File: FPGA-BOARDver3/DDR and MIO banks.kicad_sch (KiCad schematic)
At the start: 1 part, among them U1 XC7Z020-1CLG400I__

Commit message: spdif fpga bansks
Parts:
- added C4: 100nF, footprints:C_0402, symbol Device:C
- added C5, C8, C9: 10nF, footprints:C_0402, symbol Device:C
- added J4: Conn_01x04_Pin, footprints:CONN_PZ254V-11-04P_XFC, symbol Connector:Conn_01x04_Pin
- added J5, J8: Conn_01x02_Pin, footprints:CONN_PZ254V-11-02P_02P_XFC, symbol Connector:Conn_01x02_Pin
- added R17, R18, R19, R20: 10K 1%, footprints:R_0402, symbol Device:R_US
- added R36, R37, R38, R40, R42, R48, R49: 20K, footprints:R_0402, symbol Device:R_US
- added R39, R41, R43, R44, R45, R46, R47: 1K, footprints:R_0402, symbol Device:R_US
- added R4: 40.2, footprints:R_0402, symbol Device:R_US
- added R5, R6, R7: 80.6 1%, footprints:R_0402, symbol Device:R_US
- added R50, R51: 49.9, footprints:R_0402, symbol Device:R_US
- added R8: 40.2 1%, footprints:R_0402, symbol Device:R_US
- added S2: PTS645SK50SMTR92LFS, footprints:SW_PTS645SK50SMTR92LFS, symbol PTS645SK50SMTR92LFS:PTS645SK50SMTR92LFS
- added U2: DSC1122CI5-050.0000T, footprints:VDFN6_3P2X2P5_MCH, symbol 2025-04-06_19-32-54:DSC1122CI5-050.0000T
- added U3: NC7WZ07P6X, footprints:NC7WZ07P6X, symbol NC7WZ07P6X:NC7WZ07P6X
- U1: footprint footprints:CLG400_ZYNQ-7000_AMD -> XC7Z020-1CLG400I:CLG400_ZYNQ-7000_AMD
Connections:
- net DDR3_DM1: now reaches U1.A1 (PS_DDR_DM0_502)
- net DDR3_D15: now reaches U1.A2 (PS_DDR_DQ2_502)
- net DDR3_D13: now reaches U1.A4 (PS_DDR_DQ3_502)
- net DDR3_DQS1_N: now reaches U1.B2 (PS_DDR_DQS_N0_502)
- net DDR3_D12: now reaches U1.B3 (PS_DDR_DQ1_502)
- net DDR3_RESET: now reaches U1.B4 (PS_DDR_DRST_B_502)
- net DDR3_D14: now reaches U1.C1 (PS_DDR_DQ6_502)
- net DDR3_DQS1_P: now reaches U1.C2 (PS_DDR_DQS_P0_502)
- net DDR3_D11: now reaches U1.C3 (PS_DDR_DQ0_502)
- net DDR3_D10: now reaches U1.D1 (PS_DDR_DQ5_502)
- net DDR3_D9: now reaches U1.D3 (PS_DDR_DQ4_502)
- net DDR3_A13: now reaches U1.D4 (PS_DDR_A13_502)
- net DDR3_D8: now reaches U1.E1 (PS_DDR_DQ7_502)
- net DDR3_D2: now reaches U1.E2 (PS_DDR_DQ8_502)
- net DDR3_D0: now reaches U1.E3 (PS_DDR_DQ9_502)
- net DDR3_A12: now reaches U1.E4 (PS_DDR_A12_502)
- net DDR3_DM0: now reaches U1.F1 (PS_DDR_DM1_502)
- net DDR3_DQS0_N: now reaches U1.F2 (PS_DDR_DQS_N1_502)
- net DDR3_A14: now reaches U1.F4 (PS_DDR_A14_502)
- net DDR3_A10: now reaches U1.F5 (PS_DDR_A10_502)
- net DDR3_DQS0_P: now reaches U1.G2 (PS_DDR_DQS_P1_502)
- net DDR3_D6: now reaches U1.G3 (PS_DDR_DQ10_502)
- net DDR3_A11: now reaches U1.G4 (PS_DDR_A11_502)
- net at U1.G5 (PS_DDR_VRN_502): now also R6.2
- net DDR3_D3: now reaches U1.H1 (PS_DDR_DQ14_502)
- net DDR3_D7: now reaches U1.H2 (PS_DDR_DQ13_502)
- net DDR3_D1: now reaches U1.H3 (PS_DDR_DQ11_502)
- net at U1.H5 (PS_DDR_VRP_502): now also R7.2
- net DDR3_VREF: now reaches U1.H6 (PS_DDR_VREF0_502)
- net DDR3_VREF: now also U1.P6 (PS_DDR_VREF1_502), C4.1, C5.1, R17.2, R20.1
- net DDR3_D5: now reaches U1.J1 (PS_DDR_DQ15_502)
- net DDR3_D4: now reaches U1.J3 (PS_DDR_DQ12_502)
- net DDR3_A9: now reaches U1.J4 (PS_DDR_A9_502)
- net DDR3_BA2: now reaches U1.J5 (PS_DDR_BA2_502)
- net DDR3_A8: now reaches U1.K1 (PS_DDR_A8_502)
- net DDR3_A1: now reaches U1.K2 (PS_DDR_A1_502)
- net DDR3_A3: now reaches U1.K3 (PS_DDR_A3_502)
- net DDR3_A7: now reaches U1.K4 (PS_DDR_A7_502)
- net DDR3_A5: now reaches U1.L1 (PS_DDR_A5_502)
- net DDR3_CK_P: now reaches U1.L2 (PS_DDR_CKP_502)
- net DDR3_CK_P: now also R5.1
- net DDR3_A6: now reaches U1.L4 (PS_DDR_A6_502)
- net DDR3_BA0: now reaches U1.L5 (PS_DDR_BA0_502)
- net DDR3_CK_N: now reaches U1.M2 (PS_DDR_CKN_502)
- net DDR3_CK_N: now also R5.2
- net DDR3_A2: now reaches U1.M3 (PS_DDR_A2_502)
- net DDR3_A4: now reaches U1.M4 (PS_DDR_A4_502)
- net DDR3_WE: now reaches U1.M5 (PS_DDR_WE_B_502)
- net DDR3_CS: now reaches U1.N1 (PS_DDR_CS_B_502)
- net DDR3_A0: now reaches U1.N2 (PS_DDR_A0_502)
- net DDR3_CK0: now reaches U1.N3 (PS_DDR_CKE_502)
- net DDR3_ODT0: now reaches U1.N5 (PS_DDR_ODT_502)
- net DDR3_RAS: now reaches U1.P4 (PS_DDR_RAS_B_502)
- net DDR3_CAS: now reaches U1.P5 (PS_DDR_CAS_B_502)
- net DDR3_BA1: now reaches U1.R4 (PS_DDR_BA1_502)
- net USBHOST_DATA5: now reaches U1.A10 (PS_MIO37_501)
- net USBHOST_CLK: now reaches U1.A11 (PS_MIO36_501)
- net USBHOST_DATA2: now reaches U1.A12 (PS_MIO34_501)
- net USBHOST_DATA0: now reaches U1.A14 (PS_MIO32_501)
- net ETH_RXD3: now reaches U1.A15 (PS_MIO26_501)
- net ETH_RXD1: now reaches U1.A16 (PS_MIO24_501)
- net ETH_TXD3: now reaches U1.A17 (PS_MIO20_501)
- net ETH_TXCLK: now reaches U1.A19 (PS_MIO16_501)
- net SD_D1: now reaches U1.A9 (PS_MIO43_501)
- net PS_RST: now reaches U1.B10 (PS_SRST_B_501)
- net PS_RST: now also R43.2, R44.2, U3.3 (A2)
- net SD_CD: now reaches U1.B14 (PS_MIO47_501)
- net SD_D3: now reaches U1.B15 (PS_MIO45_501)
- net ETH_RXCK: now reaches U1.B17 (PS_MIO22_501)
- net ETH_TXD1: now reaches U1.B18 (PS_MIO18_501)
- net ETH_MDC: now reaches U1.C10 (PS_MIO52_501)
- net ETH_MDIO: now reaches U1.C11 (PS_MIO53_501)
- net USBHOST_DIR: now reaches U1.C13 (PS_MIO29_501)
- net USBHOST_STP: now reaches U1.C15 (PS_MIO30_501)
- net USBHOST_DATA4: now reaches U1.C16 (PS_MIO28_501)
- net SD_CMD: now reaches U1.C17 (PS_MIO41_501)
- net USBHOST_DATA7: now reaches U1.C18 (PS_MIO39_501)
- net ETH_TXD2: now reaches U1.D10 (PS_MIO19_501)
- net ETH_RXD0: now reaches U1.D11 (PS_MIO23_501)
- net ETH_RXCTL: now reaches U1.D13 (PS_MIO27_501)
- net at U1.D14 (PS_MIO40_501): now also R8.1
- net USBHOST_DATA1: now reaches U1.D15 (PS_MIO33_501)
- net USBHOST_RESETN: now reaches U1.D16 (PS_MIO46_501)
- net VREF0V9: now reaches U1.E11 (PS_MIO_VREF_501)
- net VREF0V9: now also C8.1, R18.2, R19.1
- net SD_D0: now reaches U1.E12 (PS_MIO42_501)
- net USBHOST_DATA6: now reaches U1.E13 (PS_MIO38_501)
- net ETH_TXD0: now reaches U1.E14 (PS_MIO17_501)
- net USBHOST_NXT: now reaches U1.E16 (PS_MIO31_501)
- net USBHOST_DATA3: now reaches U1.F12 (PS_MIO35_501)
- net SD_D2: now reaches U1.F13 (PS_MIO44_501)
- net ETH_TXCTL: now reaches U1.F14 (PS_MIO21_501)
- net ETH_RXD2: now reaches U1.F15 (PS_MIO25_501)
- net at U1.A5 (PS_MIO6_500): now also R4.1
- net SPI_DQ3/MODE0: now reaches U1.A6 (PS_MIO5_500)
- net SPI_DQ3/MODE0: now also R48.1
- net SPI_CS: now reaches U1.A7 (PS_MIO1_500)
- net ETH_RST_B: now reaches U1.B5 (PS_MIO9_500)
- net SPI_DQ2/MODE2: now reaches U1.B7 (PS_MIO4_500)
- net SPI_DQ2/MODE2: now also R49.1
- net SPI_DQ0/MODE3: now reaches U1.B8 (PS_MIO2_500)
- net SPI_DQ0/MODE3: now also R40.2
- net UART_TXD_IN: now reaches U1.C5 (PS_MIO14_500)
- net USBHOST_OC: now reaches U1.C6 (PS_MIO11_500)
- net PS_POR_B: now reaches U1.C7 (PS_POR_B_500)
- net UART_RXD_OUT: now reaches U1.C8 (PS_MIO15_500)
- net SPI_SCLK_FB/VCFG1: now reaches U1.D5 (PS_MIO8_500)
- net SPI_SCLK_FB/VCFG1: now also R36.2
- net SPIDQ1/MODE1: now reaches U1.D6 (PS_MIO3_500)
- net VCFG0: now reaches U1.D8 (PS_MIO7_500)
- net VCFG0: now also R37.2
- net CK_RST: now reaches U1.D9 (PS_MIO12_500)
- net CK_RST: now also R45.1, U3.4 (Y2)
- net PS_CLK: now reaches U1.E7 (PS_CLK_500)
- net PS_CLK: now also R50.1
- net ETH_INT_B: now reaches U1.E9 (PS_MIO10_500)
- new net: J4.3 (Pin_3), R47.2, R49.2
- new net: J8.1 (Pin_1), R41.2, R42.1
- new net: R50.2, R51.2, U2.4 (OUT)
- new net: J4.1 (Pin_1), R46.1, R48.2
- new net: R44.1, S2.1
- new net: J5.1 (Pin_1), R39.2, R40.1
- new net +1V5: R17.1, R7.1
- new net +1V8: R18.1, R43.1
- new net +3V3: C9.1, J4.4 (Pin_4), J5.2 (Pin_2), R36.1, R45.2, R46.2, U2.1 (EN), U2.6 (VDD)
- new net ETH_CLK: R51.1
- new net GNDREF: C4.2, C5.2, C8.2, C9.2, J4.2 (Pin_2), R19.2, R20.2, R37.1, R38.1, R39.1, R41.1, R47.1, R6.1, S2.3, U2.3 (GND)
- new net SD_CCLK: R8.2
- new net SPI_DQ1/MODE1: R38.2
- new net SPI_SCK_MODE4: R4.2
- new net SPI_SCK/MODE4: R42.2

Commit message: All pages complete , pi header left
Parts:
- removed S2: PTS645SK50SMTR92LFS, footprints:SW_PTS645SK50SMTR92LFS, symbol PTS645SK50SMTR92LFS:PTS645SK50SMTR92LFS
- added S2: PTS645SK50SMTR92LFS, footprints:SW_PTS645SK50SMTR92LFS, symbol PTS645SK50SMTR92LFS_:PTS645SK50SMTR92LFS
- U1: footprint XC7Z020-1CLG400I:CLG400_ZYNQ-7000_AMD -> footprints:CLG400_ZYNQ-7000_AMD
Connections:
- net GNDREF: now also S2.3
- net at R44.1: now also S2.1
- new net VCC: U3.5 (VCC)

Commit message: update
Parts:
- removed U3: NC7WZ07P6X, footprints:NC7WZ07P6X, symbol NC7WZ07P6X:NC7WZ07P6X
- added C176: 100nF, footprints:C_0402, symbol Device:C
- added U23: NC7WZ07P6X, footprints:NC7WZ07P6X, symbol NC7WZ07P6X:NC7WZ07P6X_modified
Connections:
- net +3V3: now also C176.1, U23.5 (VCC)
- net CK_RST: now also U23.4 (Y2)
- net GNDREF: now also C176.2, U23.2 (GND)
- net PS_RST: now also U23.3 (A2)
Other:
- note added: "VCC1V5"
- note added: "VCC1V8_IO"
- note added: "VCC3V3"

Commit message: schematic pages for review
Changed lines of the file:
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@@
 		(fields_autoplaced yes)
 		(property "Reference" "U23"
-			(at 267.97 155.5749 0)
-			(effects
-				(font
-					(size 1.27 1.27)
-				)
-				(justify left)
+			(at 269.24 140.97 0)
+			(effects
+				(font
+					(size 1.27 1.27)
+				)
 			)
 		)
 		(property "Value" "NC7WZ07P6X"
-			(at 267.97 158.1149 0)
-			(effects
-				(font
-					(size 1.27 1.27)
-				)
-				(justify left)
+			(at 269.24 143.51 0)
+			(effects
+				(font
+					(size 1.27 1.27)
+				)
 			)
 		)
@@
 	)
 	(symbol
+		(lib_name "NC7WZ07P6X_modified_1")
 		(lib_id "NC7WZ07P6X:NC7WZ07P6X_modified")
 		(at 246.38 146.05 0)

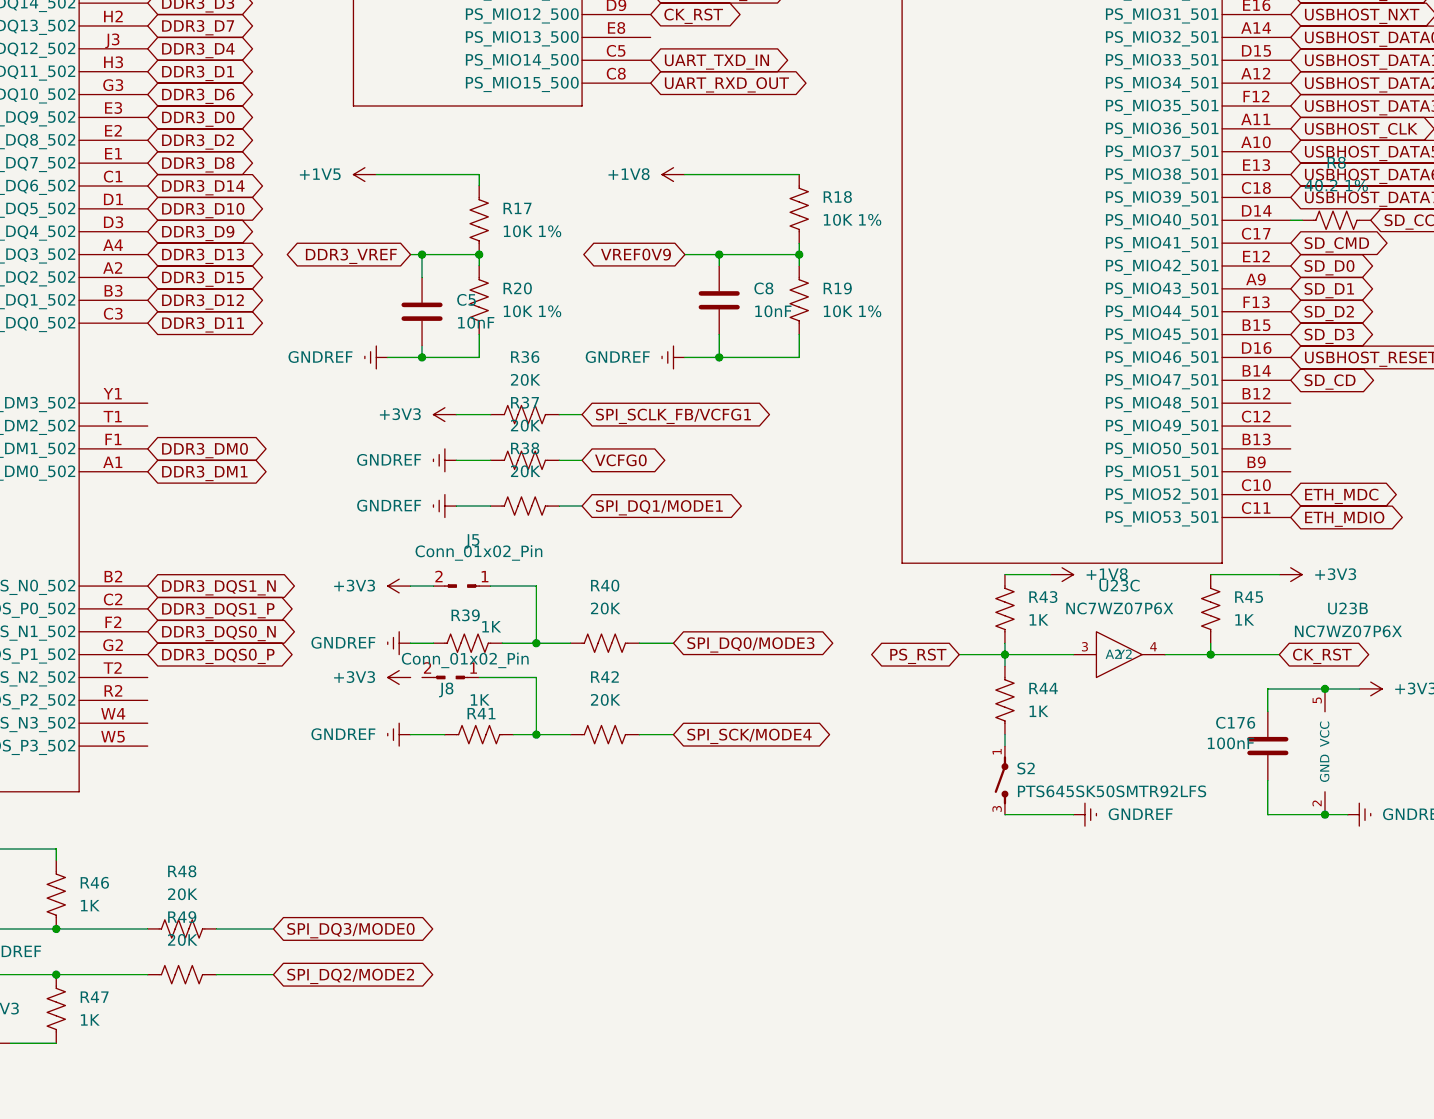
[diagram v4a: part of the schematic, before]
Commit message: added audio out and usb
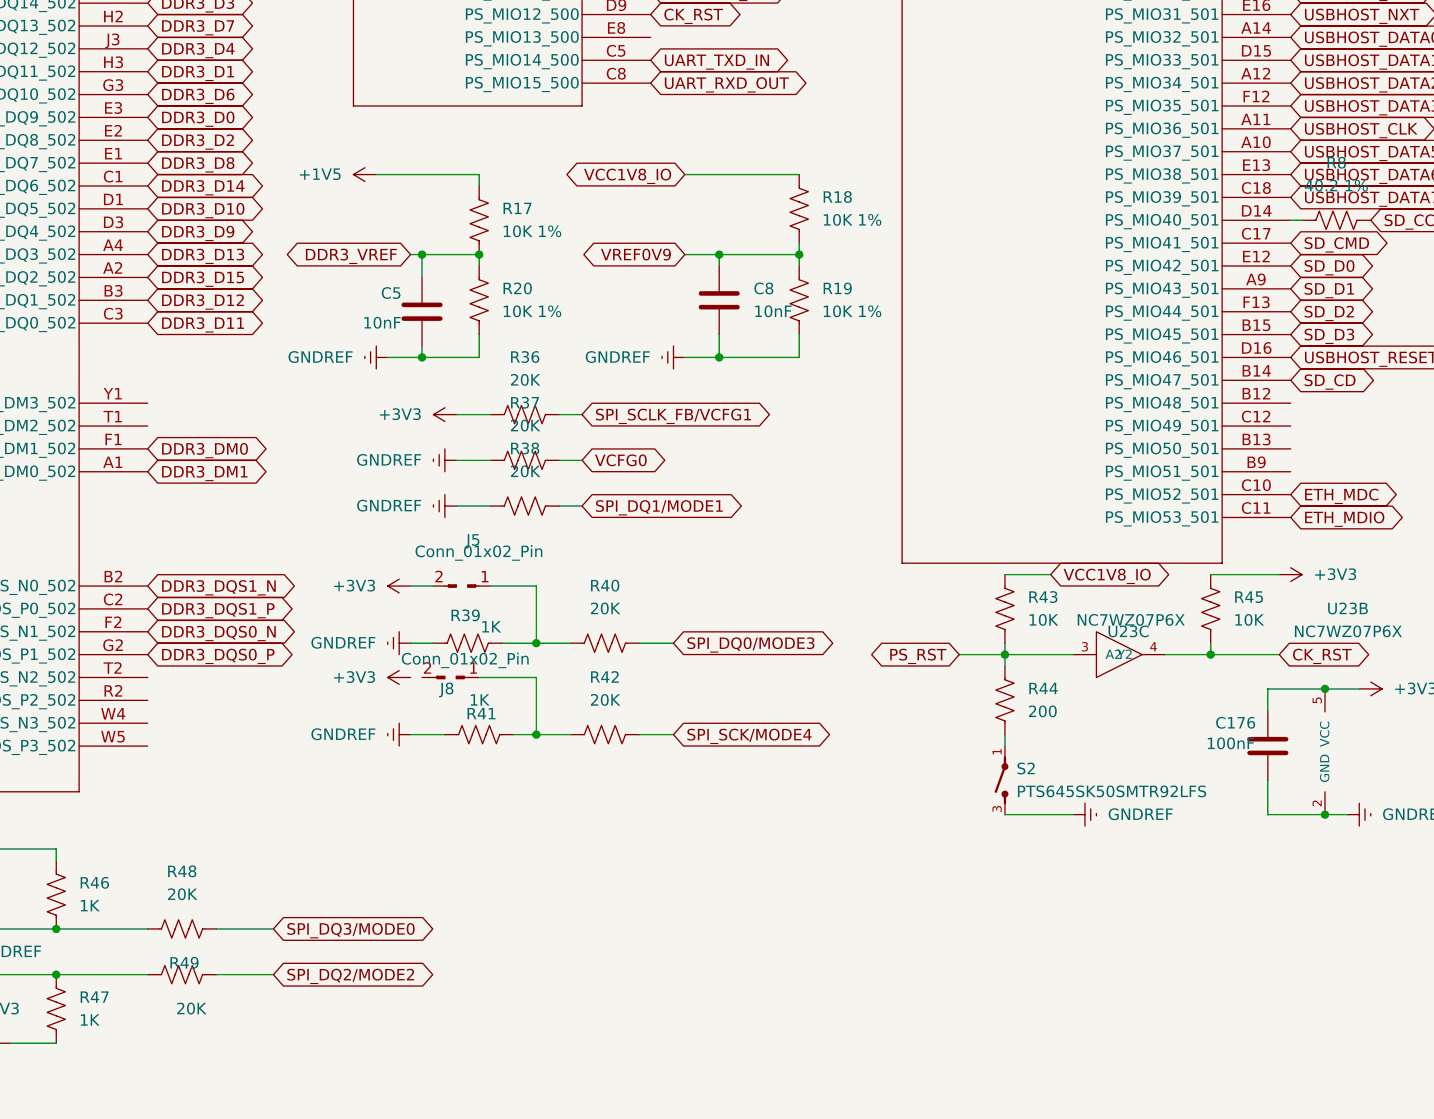
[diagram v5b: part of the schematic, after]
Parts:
- R43, R45: value 1K -> 10K
- R44: value 1K -> 200
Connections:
- net +1V8 renamed VCC1V8_IO

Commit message: updated schematic and layout
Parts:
- removed R51: 49.9, footprints:R_0402, symbol Device:R_US
- removed U2: DSC1122CI5-050.0000T, footprints:VDFN6_3P2X2P5_MCH, symbol 2025-04-06_19-32-54:DSC1122CI5-050.0000T
- added R234, R235, R236, R237, R238, R239: 40.2, footprints:R_0402, symbol Device:R_US
- added Y2: SG-8018CE_50.0000M-TJHPA, footprints:OSC_SG-8018CE_50.0000M-TJHPA, symbol SG-8018CE_50.0000M-TJHPA:SG-8018CE_50.0000M-TJHPA
- C176, C4: LCSC PN (none) -> c1525
- C5, C8, C9: LCSC PN (none) -> c15195
- J4: footprint footprints:CONN_PZ254V-11-04P_XFC -> footprints:PinHeader_1x04_P2.54mm_Vertical; LCSC PN (none) -> digi/mouser
- J5, J8: footprint footprints:CONN_PZ254V-11-02P_02P_XFC -> footprints:PinHeader_1x02_P2.54mm_Vertical; LCSC PN (none) -> digi/mouser
- R17, R18, R19, R20, R43, R45: LCSC PN (none) -> C60490
- R36, R37, R38, R40, R42, R48, R49: LCSC PN (none) -> C93942
- R39, R41, R46, R47: LCSC PN (none) -> C106235
- R4, R8: LCSC PN (none) -> C274892
- R44: LCSC PN (none) -> C114764
- R5, R6, R7: LCSC PN (none) -> C843839
- R50: LCSC PN (none) -> C87044
- S2: LCSC PN (none) -> mouser
- U1: LCSC PN (none) -> C1519081
- U23: LCSC PN (none) -> C95342
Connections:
- net SPIDQ1/MODE1 is gone; now on net SPI_DQ1/MODE1: U1.D6 (PS_MIO3_500)
- net SPI_SCK_MODE4 is gone; now on net SPI_SCK/MODE4: R4.2
- net +3V3: now also Y2.1 (OE), Y2.4 (VCC)
- net DDR3_D0: now also U1.E2 (PS_DDR_DQ8_502); no longer U1.E3 (PS_DDR_DQ9_502)
- net DDR3_D1: now also U1.H1 (PS_DDR_DQ14_502); no longer U1.H3 (PS_DDR_DQ11_502)
- net DDR3_D10: now also U1.D3 (PS_DDR_DQ4_502); no longer U1.D1 (PS_DDR_DQ5_502)
- net DDR3_D11: now also U1.C1 (PS_DDR_DQ6_502); no longer U1.C3 (PS_DDR_DQ0_502)
- net DDR3_D14: now also U1.C3 (PS_DDR_DQ0_502); no longer U1.C1 (PS_DDR_DQ6_502)
- net DDR3_D2: now also U1.E1 (PS_DDR_DQ7_502); no longer U1.E2 (PS_DDR_DQ8_502)
- net DDR3_D3: now also U1.G3 (PS_DDR_DQ10_502); no longer U1.H1 (PS_DDR_DQ14_502)
- net DDR3_D4: now also U1.J1 (PS_DDR_DQ15_502); no longer U1.J3 (PS_DDR_DQ12_502)
- net DDR3_D5: now also U1.H3 (PS_DDR_DQ11_502); no longer U1.J1 (PS_DDR_DQ15_502)
- net DDR3_D6: now also U1.H2 (PS_DDR_DQ13_502); no longer U1.G3 (PS_DDR_DQ10_502)
- net DDR3_D7: now also U1.J3 (PS_DDR_DQ12_502); no longer U1.H2 (PS_DDR_DQ13_502)
- net DDR3_D8: now also U1.E3 (PS_DDR_DQ9_502); no longer U1.E1 (PS_DDR_DQ7_502)
- net DDR3_D9: now also U1.D1 (PS_DDR_DQ5_502); no longer U1.D3 (PS_DDR_DQ4_502)
- net ETH_TXCLK: now also R239.2; no longer U1.A19 (PS_MIO16_501)
- net ETH_TXCTL: now also R235.2; no longer U1.F14 (PS_MIO21_501)
- net ETH_TXD0: now also R234.2; no longer U1.E14 (PS_MIO17_501)
- net ETH_TXD1: now also R236.2; no longer U1.B18 (PS_MIO18_501)
- net ETH_TXD2: now also R237.2; no longer U1.D10 (PS_MIO19_501)
- net ETH_TXD3: now also R238.2; no longer U1.A17 (PS_MIO20_501)
- net GNDREF: now also Y2.2 (GND)
- net at R50.2: now also Y2.3 (OUT)
- net at R7.2: now also U1.G5 (PS_DDR_VRN_502); no longer U1.H5 (PS_DDR_VRP_502)
- net at R6.2: now also U1.H5 (PS_DDR_VRP_502); no longer U1.G5 (PS_DDR_VRN_502)
- net DDR3_CK0 renamed DDR3_CKE0
- net UART_RXD_OUT renamed UART_RXD
- net UART_TXD_IN renamed UART_TXD
- new net: R238.1, U1.A17 (PS_MIO20_501)
- new net: R239.1, U1.A19 (PS_MIO16_501)
- new net: R236.1, U1.B18 (PS_MIO18_501)
- new net: R237.1, U1.D10 (PS_MIO19_501)
- new net: R234.1, U1.E14 (PS_MIO17_501)
- new net: R235.1, U1.F14 (PS_MIO21_501)
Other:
- moved on the sheet: R50
